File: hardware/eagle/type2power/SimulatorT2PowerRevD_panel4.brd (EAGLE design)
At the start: 99.1 x 99.1 mm, 40 parts

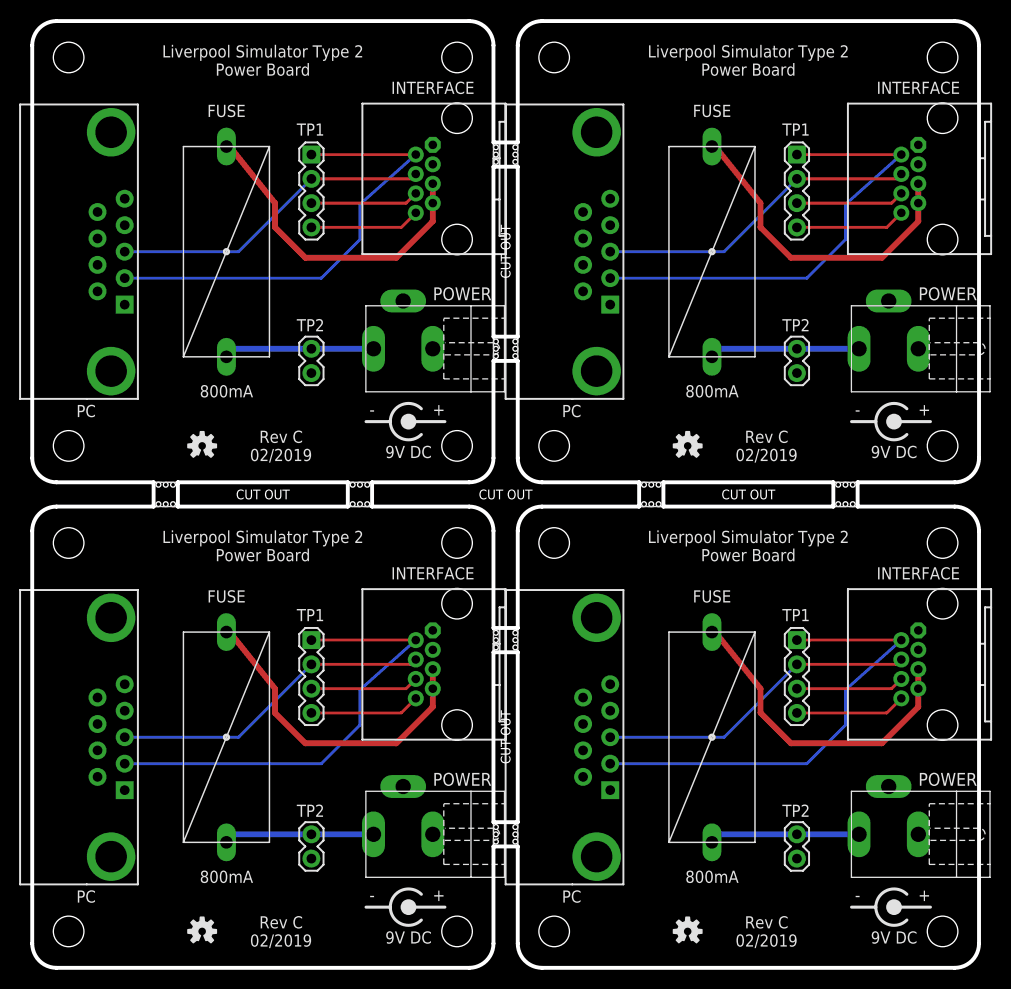
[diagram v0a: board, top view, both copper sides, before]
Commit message: Enhanced surge protection
Power Rev D, 2nd PC Rev B boards with improved surge protection,
Gerbers, Cost Estimation tool, New enclosure drilling templates.
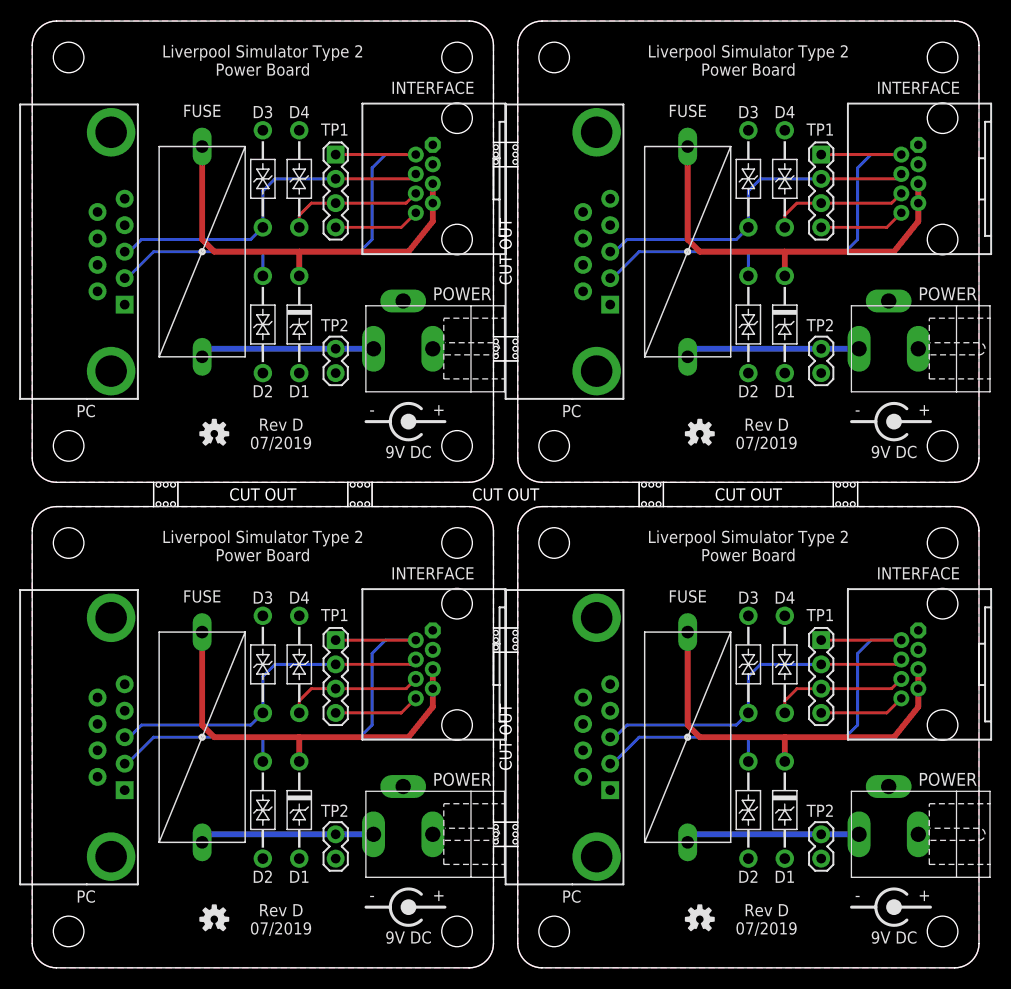
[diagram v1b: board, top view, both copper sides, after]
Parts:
- removed E$2, E$3, E$4, E$5, E$6, E$7, E$8: (no value), AIC_Custom:STAMP_HOLES
- added D1, D1_1, D1_2, D1_3: SA12A, AIC_Custom:DO41_TVS_UNI
- added D2, D2_1, D2_2, D2_3, D3, D3_1, D3_2, D3_3, D4, D4_1, D4_2, D4_3: SA15CA, AIC_Custom:DO41_TVS_BI
- E$1: device AIC_Custom:STAMP_HOLES -> AIC_Custom:OUTLINE_PANEL_4
- moved E$1 81.5 mm to (0.00, 0.00)
- moved FUSE_1 2.54 mm to (68.6, 24.1)
- moved FUSE_3 2.54 mm to (68.6, 74.9)
- moved FUSE 2.54 mm to (17.8, 24.1)
- moved FUSE_2 2.54 mm to (17.8, 74.9)
- moved TP1 2.54 mm to (31.8, 34.3)
- moved TP1_2 2.54 mm to (31.8, 85.1)
- moved TP2 2.54 mm to (31.8, 14.0)
- moved TP2_2 2.54 mm to (31.8, 64.8)
- moved TP1_1 2.54 mm to (82.5, 34.3)
- moved TP1_3 2.54 mm to (82.5, 85.1)
- moved TP2_1 2.54 mm to (82.5, 14.0)
- moved TP2_3 2.54 mm to (82.5, 64.8)
- moved LOGO1_2 1.80 mm to (19.1, 55.9)
- moved LOGO1 1.80 mm to (19.1, 5.08)
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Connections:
- net GND: now also D1.ANODE, D2.A, D3.A, D4.A
- net GND1: now also D1_1.ANODE, D2_1.A, D3_1.A, D4_1.A
- net GND2: now also D1_2.ANODE, D2_2.A, D3_2.A, D4_2.A
- net GND3: now also D1_3.ANODE, D2_3.A, D3_3.A, D4_3.A
- net RXD: now also D3.C
- net RXD1: now also D3_1.C
- net RXD2: now also D3_2.C
- net RXD3: now also D3_3.C
- net TX2: now also D4.C
- net TX21: now also D4_1.C
- net TX22: now also D4_2.C
- net TX23: now also D4_3.C
- net TXD: now also D2.C
- net TXD1: now also D2_1.C
- net TXD2: now also D2_2.C
- net TXD3: now also D2_3.C
- net VIN2: now also D1.CATHODE
- net VIN21: now also D1_1.CATHODE
- net VIN22: now also D1_2.CATHODE
- net VIN23: now also D1_3.CATHODE
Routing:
- net VIN21: track 34.4 -> 42.4 mm
- net VIN23: track 34.4 -> 42.4 mm
- net VIN22: track 34.4 -> 42.4 mm
- net VIN2: track 34.4 -> 42.4 mm
- net TX23: track 11.3 -> 14.4 mm
- net TX21: track 11.3 -> 14.4 mm
- net TX22: track 11.3 -> 14.4 mm
- net TX2: track 11.3 -> 14.4 mm
- net P82: track 11.6 -> 9.01 mm
- net P8: track 11.6 -> 9.01 mm
- net P83: track 11.6 -> 9.01 mm
- net P81: track 11.6 -> 9.01 mm
- net TXD3: track 48.7 -> 51.1 mm
- net TXD2: track 48.7 -> 51.1 mm
- net TXD1: track 48.7 -> 51.1 mm
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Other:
- board text added: "D1"
- board text added: "D2"
- board text added: "D3"
- board text added: "D4"
- board text added: "Rev D 07/2019"
- board text removed: "CUT OUT"
- board text removed: "Rev C 02/2019"
